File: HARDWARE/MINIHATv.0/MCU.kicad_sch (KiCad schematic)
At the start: 3 parts, among them U2 STM32H747IGTx

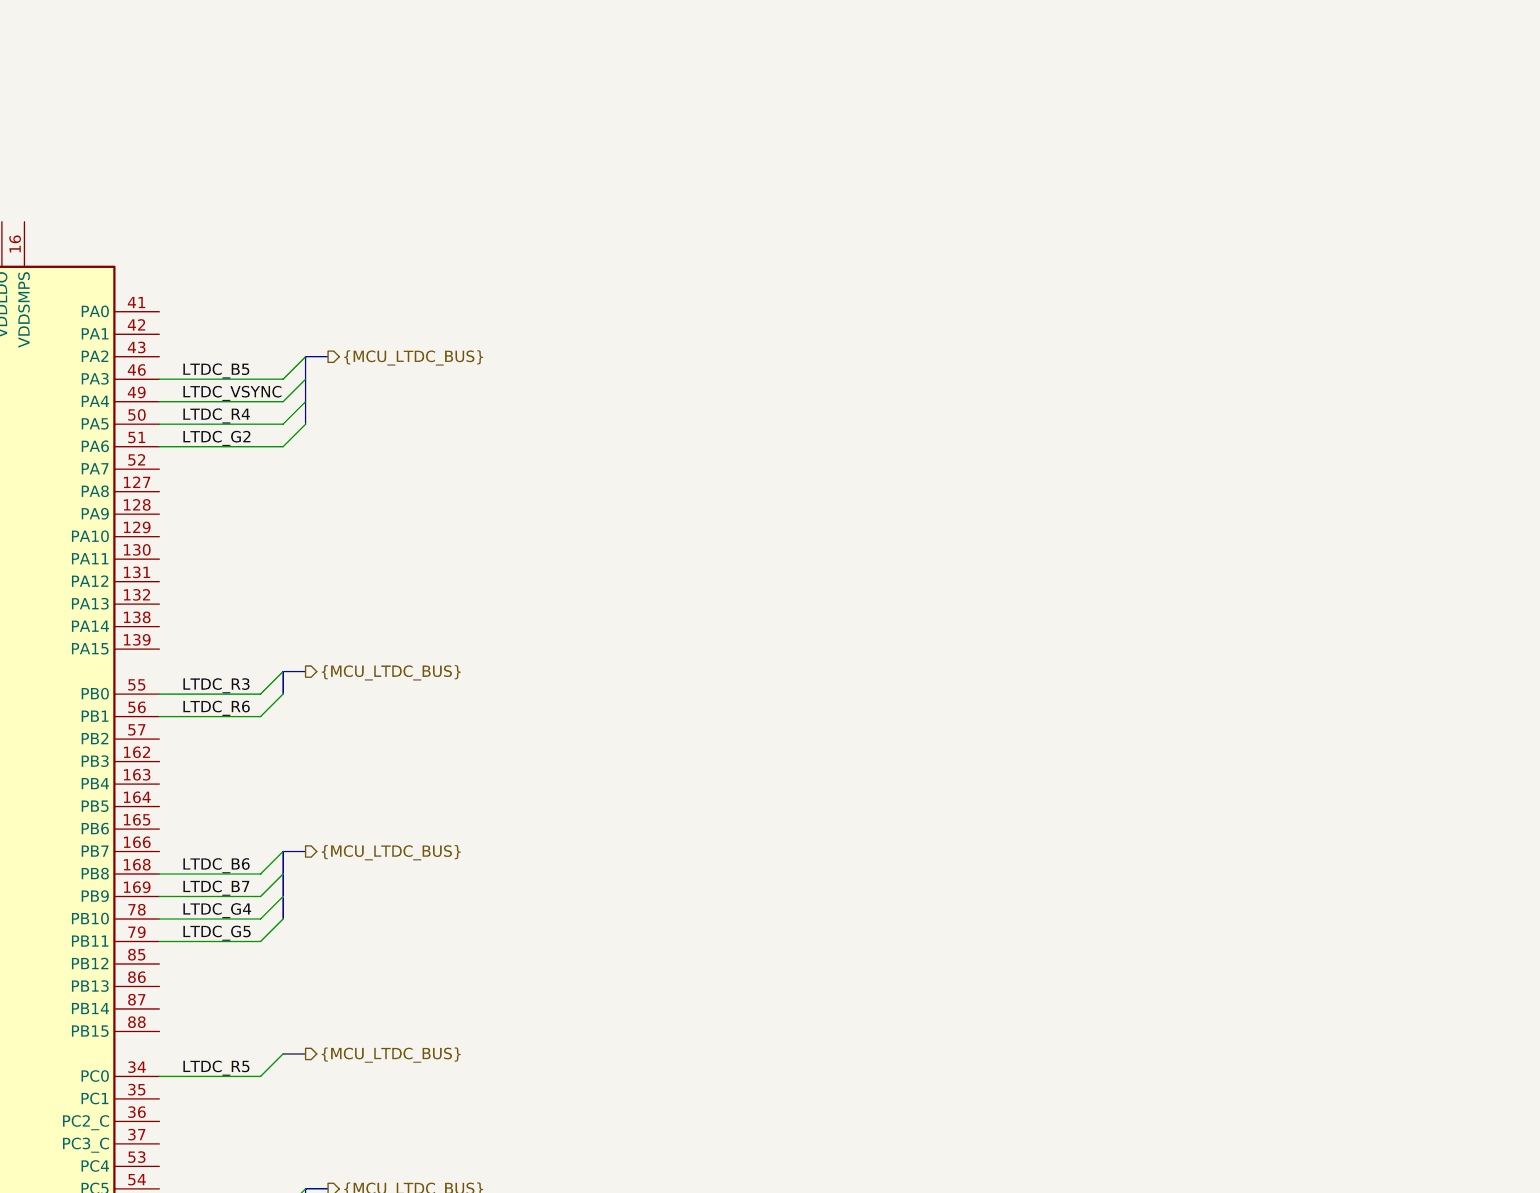
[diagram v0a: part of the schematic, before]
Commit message: FTDI for debbug added to MCU
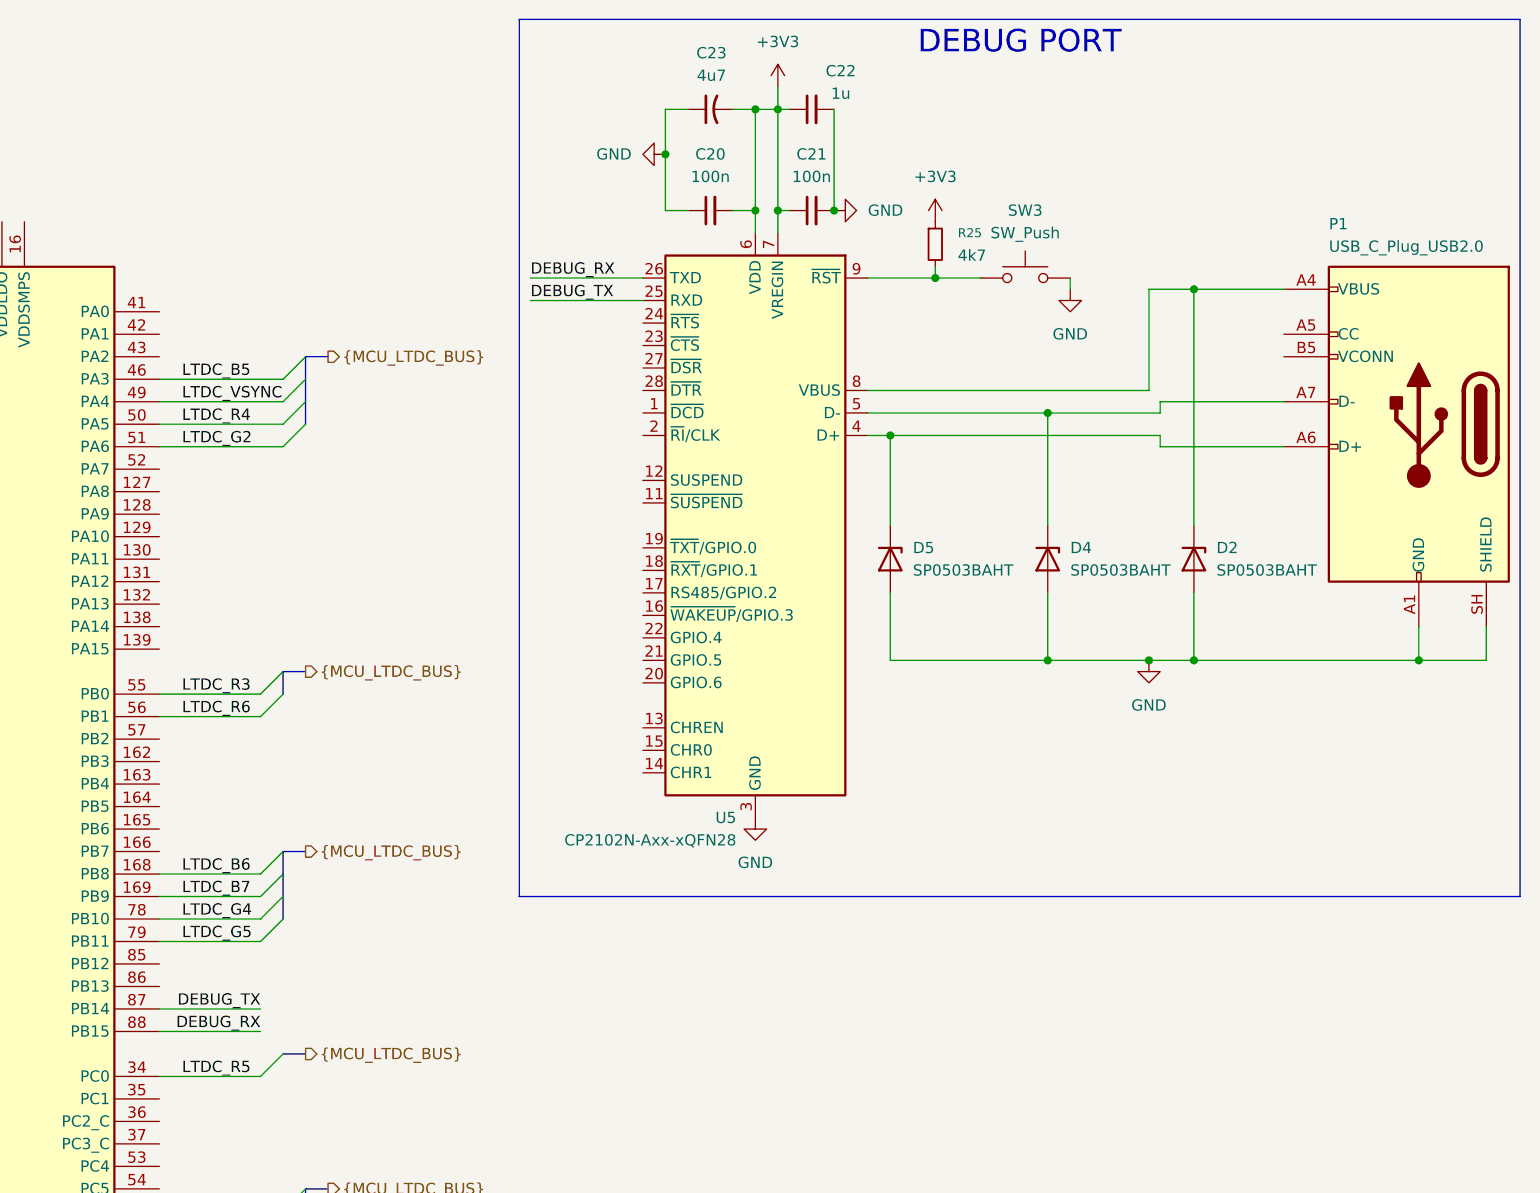
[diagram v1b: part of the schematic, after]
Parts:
- added C20, C21: 100n, symbol Device:C_Small
- added C22: 1u, symbol Device:C_Small
- added C23: 4u7, symbol Device:C_Small_US
- added D2, D4, D5: SP0503BAHT, symbol Device:D_Zener
- added P1: USB_C_Plug_USB2.0, symbol Connector:USB_C_Plug_USB2.0
- added R25: 4k7, symbol Device:R_Small
- added SW3: SW_Push, Button_Switch_SMD:SW_Push_1P1T_NO_CK_KMR2, symbol Switch:SW_Push
- added U5: CP2102N-Axx-xQFN28, Package_DFN_QFN:QFN-28-1EP_5x5mm_P0.5mm_EP3.35x3.35mm, symbol Interface_USB:CP2102N-Axx-xQFN28
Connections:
- net GND: now also C20.1, C21.2, C22.2, C23.1, D2.2 (A), D4.2 (A), D5.2 (A), P1.A1 (GND), P1.A12 (GND), P1.B1 (GND), P1.B12 (GND), P1.SH (SHIELD), SW3.2, U5.29 (GND), U5.3 (GND)
- net DEBUG_TX: now reaches U2.87 (PB14)
- net DEBUG_TX: now also U5.25 (RXD)
- net DEBUG_RX: now reaches U2.88 (PB15)
- net DEBUG_RX: now also U5.26 (TXD)
- new net: D5.1 (K), P1.A6 (D+), U5.4 (D+)
- new net: D4.1 (K), P1.A7 (D-), U5.5 (D-)
- new net: D2.1 (K), P1.A4 (VBUS), P1.A9 (VBUS), P1.B4 (VBUS), P1.B9 (VBUS), U5.8 (VBUS)
- new net: R25.2, SW3.1, U5.9 (~{RST})
- new net +3V3: C20.2, C21.1, C22.1, C23.2, R25.1, U5.6 (VDD), U5.7 (VREGIN)

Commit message: added BT sheet and created BT schemat symbol
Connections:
- net BT_TX: now reaches U2.148 (PD5)
- net BT_RX: now reaches U2.149 (PD6)
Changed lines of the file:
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@@
+	(wire
+		(pts
+			(xy 260.35 189.23) (xy 252.73 189.23)
+		)
+		(stroke
+			(width 0)
+			(type default)
+		)
+	)
 	(wire
 		(pts
@@
 		(pts
 			(xy 340.36 41.91) (xy 340.36 43.18)
+		)
+		(stroke
+			(width 0)
+			(type default)
+		)
+	)
+	(wire
+		(pts
+			(xy 260.35 191.77) (xy 252.73 191.77)
 		)
 		(stroke
@@
 		)
 	)
+	(hierarchical_label "BT_RX"
+		(shape input)
+		(at 260.35 191.77 0)
+		(effects
+			(font
+				(size 1.27 1.27)
+			)
+			(justify left)
+		)
+	)
 	(hierarchical_label "{MCU_LTDC_BUS}"
 		(shape output)
@@
 		(effects
 			(font
+				(size 1.27 1.27)
+			)
+			(justify left)
+		)
+	)
+	(hierarchical_label "BT_TX"
+		(shape input)
+		(at 260.35 189.23 0)
+		(effects
+			(font

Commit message: buses defined ind project settings, added stm antenna footprint, organized TOP
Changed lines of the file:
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@@
+		)
+	)
+	(bus
+		(pts
+			(xy 74.93 50.8) (xy 74.93 59.69)
+		)
+		(stroke
+			(width 0)
+			(type default)
 		)
 	)
@@
 	(bus
 		(pts
+			(xy 50.8 64.77) (xy 60.96 64.77)
+		)
+		(stroke
+			(width 0)
+			(type default)
+		)
+	)
+	(bus
+		(pts
 			(xy 266.7 107.95) (xy 266.7 110.49)
 		)
@@
 	(bus
 		(pts
+			(xy 50.8 58.42) (xy 67.31 58.42)
+		)
+		(stroke
+			(width 0)
+			(type default)
+		)
+	)
+	(bus
+		(pts
 			(xy 142.24 204.47) (xy 142.24 214.63)
 		)
@@
 		)
 	)
+	(bus
+		(pts
+			(xy 60.96 64.77) (xy 60.96 73.66)
+		)
+		(stroke
+			(width 0)
+			(type default)
+		)
+	)
 	(wire
 		(pts
@@
 		)
 	)
+	(bus
+		(pts
+			(xy 67.31 58.42) (xy 67.31 66.04)
+		)
+		(stroke
+			(width 0)
+			(type default)
+		)
+	)
 	(wire
 		(pts
@@
 		(pts
 			(xy 252.73 90.17) (xy 264.16 90.17)
+		)
+		(stroke
+			(width 0)
+			(type default)
+		)
+	)
+	(bus
+		(pts
+			(xy 50.8 50.8) (xy 74.93 50.8)
 		)
 		(stroke
@@
 		)
 	)
+	(hierarchical_label "QSPI"
+		(shape input)
+		(at 50.8 50.8 180)
+		(effects
+			(font
+				(size 1.27 1.27)
+			)
+			(justify right)
+		)
+	)
 	(hierarchical_label "{MCU_LTDC_BUS}"
 		(shape output)
@@
 		)
 	)
+	(hierarchical_label "RMII"
+		(shape input)
+		(at 50.8 64.77 180)
+		(effects
+			(font
+				(size 1.27 1.27)
+			)
+			(justify right)
+		)
+	)
 	(hierarchical_label "FDCAN_Tx"
 		(shape input)
@@
 		)
 	)
+	(hierarchical_label "SDIO"
+		(shape input)
+		(at 50.8 58.42 180)
+		(effects
+			(font
+				(size 1.27 1.27)
+			)
+			(justify right)
+		)
+	)

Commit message: added i2c for hdmi
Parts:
- renumbered C23 to C3, C20 to C4, C22 to C5, C21 to C6, D5 to D3, D2 to D5, R13 to R4, R14 to R5, R25 to R6, SW3 to SW1, U5 to U3
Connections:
- net LTDC_CEC: now reaches U2.139 (PA15)
- net HDMI_SCL: now reaches U2.165 (PB6)
- net HDMI_SDA: now reaches U2.166 (PB7)
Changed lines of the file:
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@@
 	(wire
 		(pts
+			(xy 264.16 105.41) (xy 269.24 105.41)
+		)
+		(stroke
+			(width 0)
+			(type default)
+		)
+	)
+	(wire
+		(pts
 			(xy 252.73 57.15) (xy 266.7 57.15)
 		)
@@
 		)
 	)
+	(wire
+		(pts
+			(xy 262.89 105.41) (xy 252.73 105.41)
+		)
+		(stroke
+			(width 0)
+			(type default)
+		)
+	)
+	(wire
+		(pts
+			(xy 262.89 102.87) (xy 269.24 102.87)
+		)
+		(stroke
+			(width 0)
+			(type default)
+		)
+	)
 	(bus
 		(pts
@@
 		)
 	)
+	(wire
+		(pts
+			(xy 264.16 105.41) (xy 264.16 107.95)
+		)
+		(stroke
+			(width 0)
+			(type default)
+		)
+	)
 	(bus
 		(pts
@@
 	(wire
 		(pts
+			(xy 262.89 102.87) (xy 262.89 105.41)
+		)
+		(stroke
+			(width 0)
+			(type default)
+		)
+	)
+	(wire
+		(pts
 			(xy 335.28 86.36) (xy 353.06 86.36)
 		)
@@
 	(wire
 		(pts
+			(xy 264.16 107.95) (xy 252.73 107.95)
+		)
+		(stroke
+			(width 0)
+			(type default)
+		)
+	)
+	(wire
+		(pts
 			(xy 276.86 184.15) (xy 271.78 184.15)
 		)
@@
 	(wire
 		(pts
+			(xy 252.73 85.09) (xy 269.24 85.09)
+		)
+		(stroke
+			(width 0)
+			(type default)
+		)
+	)
+	(wire
+		(pts
 			(xy 252.73 201.93) (xy 264.16 201.93)
 		)
@@
 		)
 	)
+	(hierarchical_label "LTDC_CEC"
+		(shape output)
+		(at 269.24 85.09 0)
+		(effects
+			(font
+				(size 1.27 1.27)
+			)
+			(justify left)
+		)
+	)
 	(hierarchical_label "FDCAN_Tx"
 		(shape input)
@@
 		)
 	)
+	(hierarchical_label "HDMI_SDA"
+		(shape input)
+		(at 269.24 105.41 0)
+		(effects
+			(font
+				(size 1.27 1.27)
+			)
+			(justify left)
+		)
+	)
 	(hierarchical_label "{MCU_LTDC_BUS}"
 		(shape output)
@@
 		)
 	)
+	(hierarchical_label "HDMI_SCL"
+		(shape input)
+		(at 269.24 102.87 0)
+		(effects
+			(font
+				(size 1.27 1.27)
+			)
+			(justify left)
+		)
+	)
 	(hierarchical_label "{MCU_LTDC_BUS}"
 		(shape output)
@@
 		(in_pos_files yes)
 		(dnp no)
-		(property "Reference" "U5"
+		(property "Reference" "U3"
 			(at 317.8967 104.14 0)
 			(show_name no)
@@
 			(project "MINIHATv.0"
 				(path "/19041ef4-1d16-4363-8780-721ad9f20b33/cd5db47d-2b35-4622-a88b-05ef4e37f3d0"
-					(reference "U5")
+					(reference "U3")
 					(unit 1)
 				)
@@
 		(dnp no)
 		(fields_autoplaced yes)
-		(property "Reference" "#PWR038"
+		(property "Reference" "#PWR012"
 			(at 322.58 25.4 0)
 			(hide yes)
@@
 			(project "MINIHATv.0"
 				(path "/19041ef4-1d16-4363-8780-721ad9f20b33/cd5db47d-2b35-4622-a88b-05ef4e37f3d0"
-					(reference "#PWR038")
+					(reference "#PWR012")
 					(unit 1)
 				)
@@
 		(dnp no)
 		(fields_autoplaced yes)
-		(property "Reference" "#PWR037"
+		(property "Reference" "#PWR010"
 			(at 303.53 29.21 0)
 			(hide yes)
@@
 			(project "MINIHATv.0"
 				(path "/19041ef4-1d16-4363-8780-721ad9f20b33/cd5db47d-2b35-4622-a88b-05ef4e37f3d0"
-					(reference "#PWR037")
+					(reference "#PWR010")
 					(unit 1)
 				)
@@
 		(dnp no)
 		(fields_autoplaced yes)
-		(property "Reference" "C20"
+		(property "Reference" "C4"
 			(at 314.9663 29.21 90)
 			(show_name no)
@@
 			(project "MINIHATv.0"
 				(path "/19041ef4-1d16-4363-8780-721ad9f20b33/cd5db47d-2b35-4622-a88b-05ef4e37f3d0"
-					(reference "C20")
+					(reference "C4")
 					(unit 1)
 				)
@@
 		(dnp no)
 		(fields_autoplaced yes)
-		(property "Reference" "#PWR040"
+		(property "Reference" "#PWR014"
 			(at 340.36 40.64 0)
 			(hide yes)
@@
 			(project "MINIHATv.0"
 				(path "/19041ef4-1d16-4363-8780-721ad9f20b33/cd5db47d-2b35-4622-a88b-05ef4e37f3d0"
-					(reference "#PWR040")
+					(reference "#PWR014")
 					(unit 1)
 				)
@@
 		(dnp no)
 		(fields_autoplaced yes)
-		(property "Reference" "C23"
+		(property "Reference" "C3"
 			(at 315.087 17.78 90)
 			(show_name no)
@@
 			(project "MINIHATv.0"
 				(path "/19041ef4-1d16-4363-8780-721ad9f20b33/cd5db47d-2b35-4622-a88b-05ef4e37f3d0"
-					(reference "C23")
+					(reference "C3")
 					(unit 1)
 				)
@@
 		(dnp no)
 		(fields_autoplaced yes)
-		(property "Reference" "#PWR041"
+		(property "Reference" "#PWR015"
 			(at 355.6 50.8 0)
 			(hide yes)
@@
 			(project "MINIHATv.0"
 				(path "/19041ef4-1d16-4363-8780-721ad9f20b33/cd5db47d-2b35-4622-a88b-05ef4e37f3d0"
-					(reference "#PWR041")
+					(reference "#PWR015")
 					(unit 1)
 				)
@@
 		(dnp no)
 		(fields_autoplaced yes)
-		(property "Reference" "#PWR036"
+		(property "Reference" "#PWR013"
 			(at 335.28 35.56 0)
 			(hide yes)
@@
 			(project "MINIHATv.0"
 				(path "/19041ef4-1d16-4363-8780-721ad9f20b33/cd5db47d-2b35-4622-a88b-05ef4e37f3d0"
-					(reference "#PWR036")
+					(reference "#PWR013")
 					(unit 1)
 				)
@@
 		(dnp no)
 		(fields_autoplaced yes)
-		(property "Reference" "R14"
+		(property "Reference" "R5"
 			(at 267.97 177.8 90)
 			(show_name no)
@@
 			(project "MINIHATv.0"
 				(path "/19041ef4-1d16-4363-8780-721ad9f20b33/cd5db47d-2b35-4622-a88b-05ef4e37f3d0"
-					(reference "R14")
+					(reference "R5")
 					(unit 1)
 				)
@@
 		(dnp no)
 		(fields_autoplaced yes)
-		(property "Reference" "D5"
+		(property "Reference" "D3"
 			(at 337.82 73.6599 90)
 			(show_name no)
@@
 			(project "MINIHATv.0"
 				(path "/19041ef4-1d16-4363-8780-721ad9f20b33/cd5db47d-2b35-4622-a88b-05ef4e37f3d0"
-					(reference "D5")
+					(reference "D3")
 					(unit 1)
 				)
@@
 		(in_pos_files yes)
 		(dnp no)
-		(property "Reference" "C22"
+		(property "Reference" "C5"
 			(at 329.692 19.812 90)
 			(show_name no)
@@
 			(project "MINIHATv.0"
 				(path "/19041ef4-1d16-4363-8780-721ad9f20b33/cd5db47d-2b35-4622-a88b-05ef4e37f3d0"
-					(reference "C22")
+					(reference "C5")
 					(unit 1)
 				)
@@
 		(dnp no)
 		(fields_autoplaced yes)
-		(property "Reference" "C21"
+		(property "Reference" "C6"
 			(at 326.3963 29.21 90)
 			(show_name no)
@@
 			(project "MINIHATv.0"
 				(path "/19041ef4-1d16-4363-8780-721ad9f20b33/cd5db47d-2b35-4622-a88b-05ef4e37f3d0"
-					(reference "C21")
+					(reference "C6")
 					(unit 1)
 				)
@@
 		(dnp no)
 		(fields_autoplaced yes)
-		(property "Reference" "R25"
+		(property "Reference" "R6"
 			(at 342.9 38.0999 0)
 			(show_name no)
@@
 			(project "MINIHATv.0"
 				(path "/19041ef4-1d16-4363-8780-721ad9f20b33/cd5db47d-2b35-4622-a88b-05ef4e37f3d0"
-					(reference "R25")
+					(reference "R6")
 					(unit 1)
 				)
@@
 		(dnp no)
 		(fields_autoplaced yes)
-		(property "Reference" "#PWR017"
+		(property "Reference" "#PWR09"
 			(at 205.74 246.38 0)
 			(hide yes)
@@
 			(project "MINIHATv.0"
 				(path "/19041ef4-1d16-4363-8780-721ad9f20b33/cd5db47d-2b35-4622-a88b-05ef4e37f3d0"
-					(reference "#PWR017")
+					(reference "#PWR09")
 					(unit 1)
 				)
@@
 		(dnp no)
 		(fields_autoplaced yes)
-		(property "Reference" "R13"
+		(property "Reference" "R4"
 			(at 267.97 167.64 90)
 			(show_name no)
@@
 			(project "MINIHATv.0"
 				(path "/19041ef4-1d16-4363-8780-721ad9f20b33/cd5db47d-2b35-4622-a88b-05ef4e37f3d0"
-					(reference "R13")
+					(reference "R4")
 					(unit 1)
 				)
@@
 		(dnp no)
 		(fields_autoplaced yes)
-		(property "Reference" "#PWR039"
+		(property "Reference" "#PWR011"
 			(at 320.04 110.49 0)
 			(hide yes)
@@
 			(project "MINIHATv.0"
 				(path "/19041ef4-1d16-4363-8780-721ad9f20b33/cd5db47d-2b35-4622-a88b-05ef4e37f3d0"
-					(reference "#PWR039")
+					(reference "#PWR011")
 					(unit 1)
 				)
@@
 		(dnp no)
 		(fields_autoplaced yes)
-		(property "Reference" "SW3"
+		(property "Reference" "SW1"
 			(at 350.52 35.56 0)
 			(show_name no)
@@
 			(project "MINIHATv.0"
 				(path "/19041ef4-1d16-4363-8780-721ad9f20b33/cd5db47d-2b35-4622-a88b-05ef4e37f3d0"
-					(reference "SW3")
+					(reference "SW1")
 					(unit 1)
 				)
@@
 		(dnp no)
 		(fields_autoplaced yes)
-		(property "Reference" "#PWR035"
+		(property "Reference" "#PWR016"
 			(at 364.49 92.71 0)
 			(hide yes)
@@
 			(project "MINIHATv.0"
 				(path "/19041ef4-1d16-4363-8780-721ad9f20b33/cd5db47d-2b35-4622-a88b-05ef4e37f3d0"
-					(reference "#PWR035")
+					(reference "#PWR016")
 					(unit 1)
 				)
@@
 		(dnp no)
 		(fields_autoplaced yes)
-		(property "Reference" "D2"
+		(property "Reference" "D5"
 			(at 372.11 73.6599 90)
 			(show_name no)
@@
 			(project "MINIHATv.0"
 				(path "/19041ef4-1d16-4363-8780-721ad9f20b33/cd5db47d-2b35-4622-a88b-05ef4e37f3d0"
-					(reference "D2")
+					(reference "D5")
 					(unit 1)
 				)
